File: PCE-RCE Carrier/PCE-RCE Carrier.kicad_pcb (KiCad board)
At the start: 2 copper layers, 38 x 39.5 mm, 38 parts, among them J1 Conn_01x02, J10 Conn_01x06_Pin, J11 Conn_01x02, J2 XT60PW-F, J3 XT30UPB-M, J4 XT60PW-F, J5 DF40C-34DP-0.4V_58_, J6 PRT-16766, J7 DF40C-34DP-0.4V_58_, J9 XT30UPB-M, Q1 SP2002KNC, U2 TPS54302DDCR, U3 BD6222HFP-TR, U4 LMR51430, U5 BD6222HFP-TR

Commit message: more silkscreen and layout touch up
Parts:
- added G***: LOGO, WURocketry_logo:WURocketry_logo, B.Cu at (152.0, 64.0)
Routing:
- net Net-(J10-Pin_2): track 0.00 -> 2.51 mm
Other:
- board text added: "+"
- board text added: "3V3"
- board text added: "<BAT"
- board text added: "<SW"
- board text added: "CS"
- board text added: "Carrier"
- board text added: "Department of Electrical and Systems Engineering Washington University McKelvey School of Engineering"
- board text added: "GND"
- board text added: "J1 SOLENOID"
- board text added: "J11 ANALOGUE PORT"
- board text added: "M1"
- board text added: "M2"
- board text added: "MISO"
- board text added: "MOSI"
- board text added: "PCE"
- board text added: "QWIIC I2C"
- board text added: "SCLK"
- board text added: "This is a haiku, We should cut the Airbrakes team, Live laugh love rocket"
- board text added: "WURocketry 2026-2027"
- board text added: "for Airdahl Flight Computer"

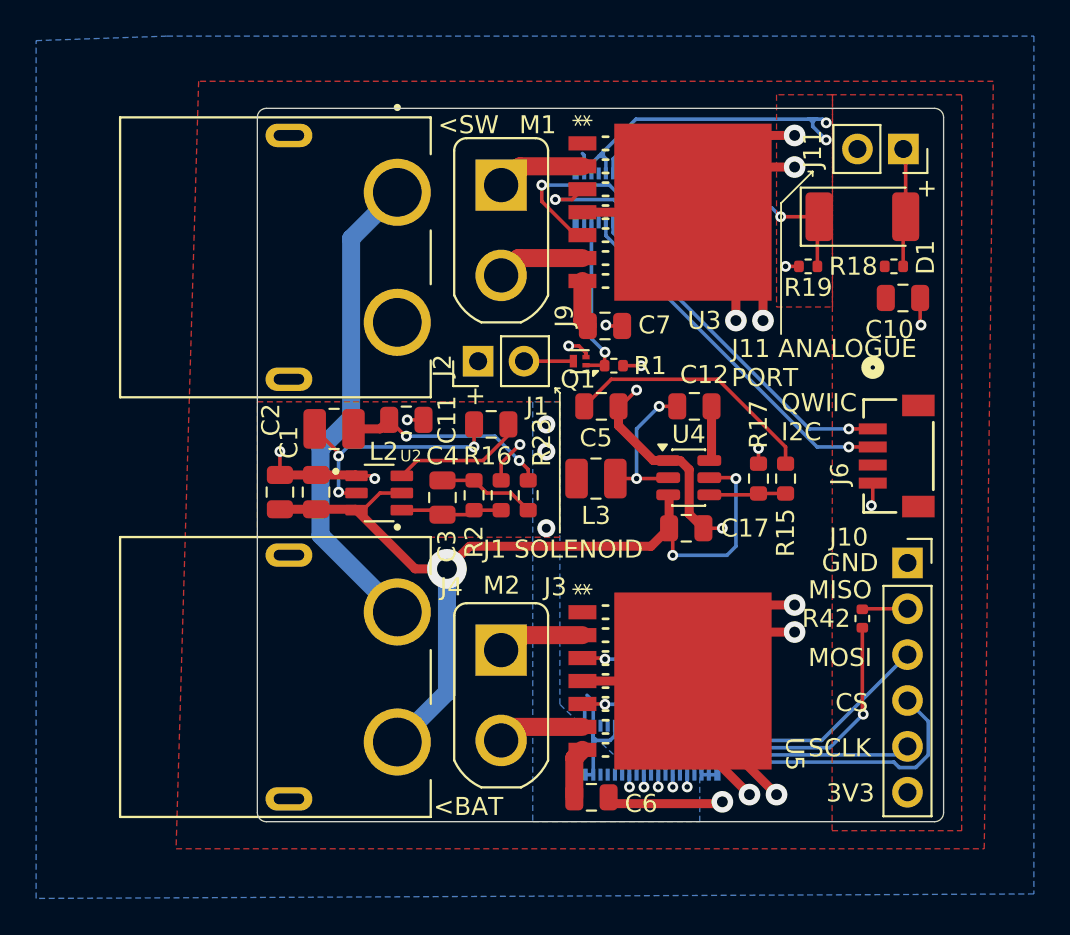
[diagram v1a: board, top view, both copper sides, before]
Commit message: DRC changes and updated fab files
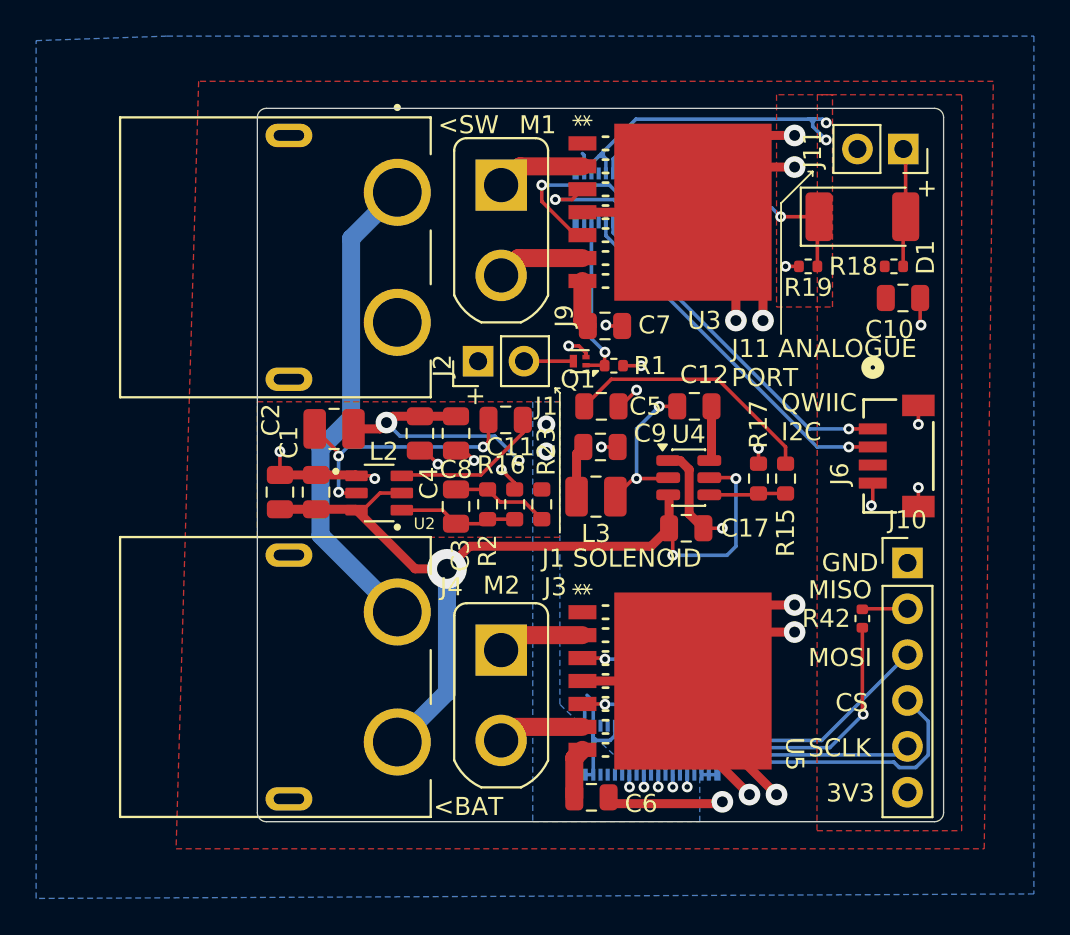
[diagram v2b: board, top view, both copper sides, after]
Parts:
- added C8: 22u, Capacitor_SMD:C_0805_2012Metric, F.Cu at (133.0, 72.0)
- added C9: 22u 25V, Capacitor_SMD:C_0805_2012Metric, F.Cu at (141.0, 72.8)
- C4: value 44u -> 22u
- C5: value 44u 25V -> 22u 25V
- J10: footprint Connector_PinSocket_2.54mm:PinSocket_1x06_P2.54mm_Vertical -> Connector_PinHeader_2.54mm:PinHeader_1x06_P2.54mm_Vertical
- moved C4 1.06 mm to (131.0, 72.0), turned to -90 degrees
- moved L3 1.00 mm to (140.8, 75.5)
- moved C3 0.90 mm to (133.0, 76.0)
- moved R16 0.90 mm to (136.2, 75.9)
- moved R2 0.90 mm to (134.8, 75.9)
- moved R23 0.90 mm to (137.8, 75.9)
- moved C11 0.84 mm to (135.8, 71.2)
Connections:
- J6 pad 5: (no net) -> GND
- J6 pad 6: (no net) -> GND
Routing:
- net +12V: track 19.7 -> 22.6 mm
- net +3V3_REG: track 15.0 -> 17.6 mm, vias 10 -> 9
- net GND: track 124.5 -> 123.4 mm, vias 22 -> 26
- net Net-(U2-BOOT): track 7.43 -> 8.41 mm
- net Net-(U2-FB): track 5.71 -> 6.66 mm
- net Net-(U2-SW): track 14.0 -> 14.9 mm
